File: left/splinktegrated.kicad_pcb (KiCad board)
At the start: 4 copper layers, 72.5 x 88.4 mm, 81 parts, among them J1 USB_C_Receptacle_USB2.0, J10 NA_Ribbon, J13 Conn_01x01_Socket, J14 Cirque, J15 Conn_01x01_Socket, J16 Conn_01x01_Socket, J17 Conn_01x01_Socket, J18 USB_C_Receptacle_USB2.0, J19 Conn_01x01_Socket, J20 Conn_01x01_Socket, J5 Conn_01x02, J6 Cirque, J7 NA_trackball, J8 NA_Ribbon, J9 NA_RGB, Q4 AO3401A, Q5 AO3401A, SW2 NA_SW_SPST, U1 RP2040, U2 USBLC6-2P6, U3 XC6210B332MR-G, U4 USBLC6-2P6, U5 W25Q128JVS, U6 74LVC1T45, Y1 Crystal_GND24

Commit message: move things
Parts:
- removed the H5008 at (173.2, 145.5)
- removed the H5008 at (165.2, 99.7)
- removed the H5008 at (160.6, 126.0)
- removed the H5008 at (131.6, 95.8)
- removed the H5008 at (137.2, 127.2)
- removed the H5008 at (122.7, 145.6)
- removed the H5008 at (130.6, 66.9)
- removed the H5008 at (172.9, 66.9)
- added ?: , , B.Cu at (151.4, 118.7)
- added G***: LOGO, LOGO, F.Cu at (167.4, 96.9)
- added H5008: NA_M4, local-libraries:mousebite, B.Cu at (139.6, 99.7)
- added H5008: NA_M4, local-libraries:mousebite, B.Cu at (131.9, 66.9)
- added H5008: NA_M4, local-libraries:mousebite, B.Cu at (174.3, 66.9)
- added H5008: NA_M4, local-libraries:mousebite, B.Cu at (144.2, 126.0)
- added H5008: NA_M4, local-libraries:mousebite, B.Cu at (173.2, 95.8)
- added H5008: NA_M4, local-libraries:mousebite, B.Cu at (182.2, 145.6)
- added H5008: NA_M4, local-libraries:mousebite, B.Cu at (167.7, 127.2)
- added H5008: NA_M4, local-libraries:mousebite, B.Cu at (131.7, 145.5)
- added J9: NA_RGB, Library:header1x03, B.Cu at (164.8, 103.7)
- added SW2: NA_SW_SPST, Library:PushSwitch, F.Cu at (166.4, 96.8)
- H1, H2, J10, J7, J8: moved to B.Cu
- moved H1 41.6 mm to (173.2, 110.0), turned to 180 degrees
- moved G*** 29.9 mm to (167.4, 96.9), turned to 180 degrees
- moved SW2 28.0 mm to (166.4, 97.0), turned to -90 degrees
- moved H2 27.6 mm to (138.6, 82.1), turned to 180 degrees
- moved D2 11.0 mm to (152.8, 86.7)
- moved D39 11.0 mm to (161.6, 88.8)
- moved F1 11.0 mm to (145.5, 87.0)
- moved F2 11.0 mm to (161.6, 85.9)
- moved FB1 11.0 mm to (156.6, 85.3)
- moved FB13 11.0 mm to (159.6, 85.9)
- moved FB14 11.0 mm to (145.4, 85.2)
- moved FB2 11.0 mm to (170.5, 85.2)
- moved J1 11.0 mm to (150.4, 75.3)
- moved J18 11.0 mm to (165.4, 75.3)
- moved Q4 11.0 mm to (166.5, 86.2)
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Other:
- board size 72.5 x 88.4 mm -> 72.6 x 88.4 mm

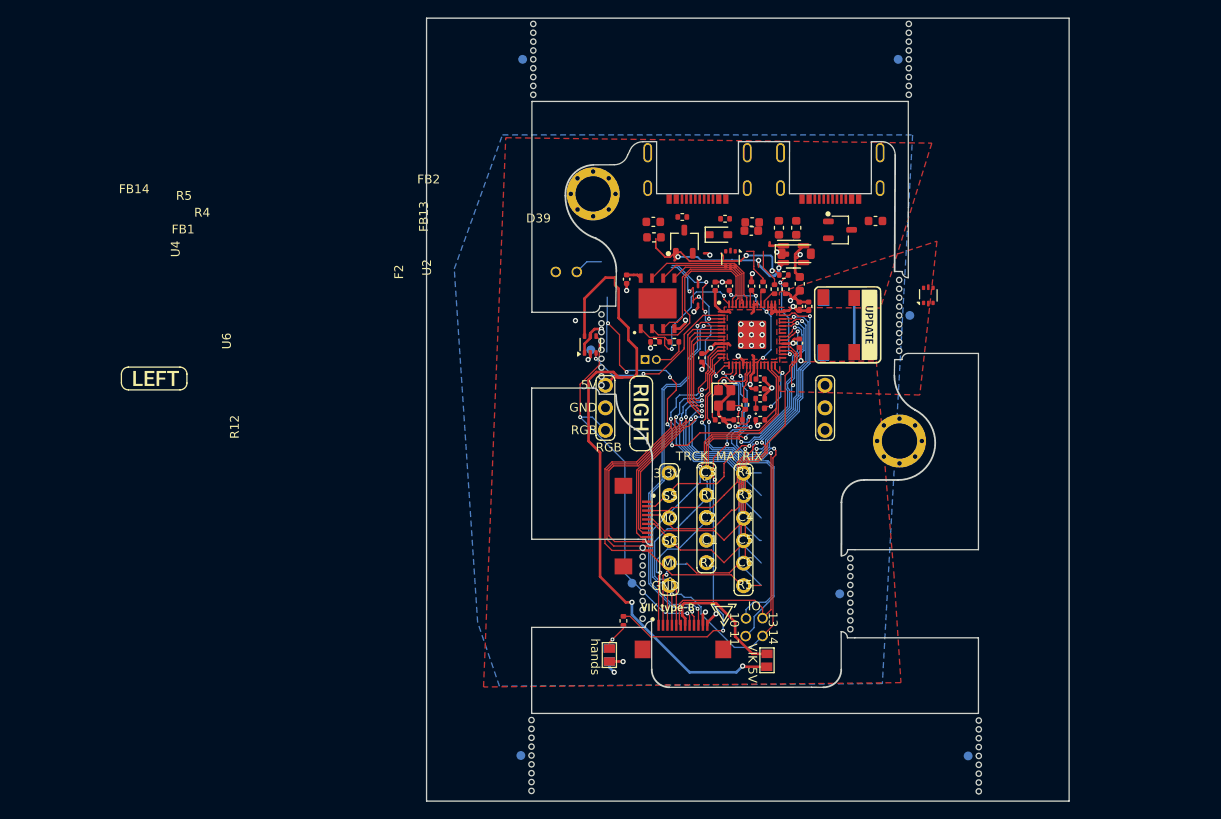
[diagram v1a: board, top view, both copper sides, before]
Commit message: route left side
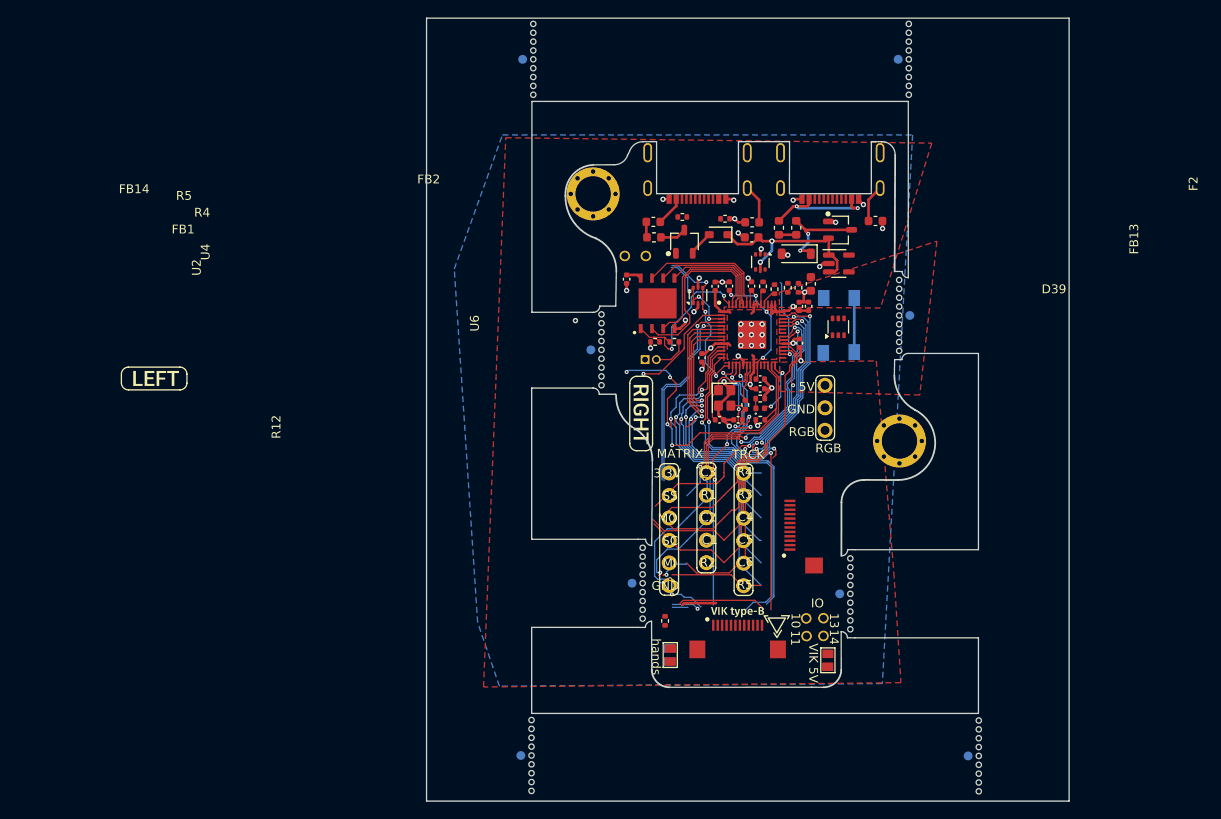
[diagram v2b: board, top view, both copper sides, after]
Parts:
- removed the G*** at (167.4, 96.9)
- removed the J9 at (140.0, 103.7)
- removed the SW2 at (166.4, 96.8)
- moved U6 28.1 mm to (166.3, 97.1)
- moved U2 26.0 mm to (150.5, 93.5)
- moved J14 18.8 mm to (162.2, 119.5), turned to 90 degrees
- moved J19 8.00 mm to (142.2, 89.1)
- moved J20 8.00 mm to (144.6, 89.1)
- moved G*** 7.91 mm to (154.9, 129.3)
- moved J15 6.88 mm to (162.7, 132.0)
- moved J16 6.88 mm to (164.6, 130.0)
- moved J17 6.88 mm to (164.6, 132.0)
- moved NA_JP5 6.88 mm to (165.1, 134.8)
- moved NA_JP7 6.88 mm to (147.3, 134.2)
- moved J13 6.80 mm to (162.7, 130.0)
- moved NA_JP6 6.80 mm to (147.2, 134.2)
- moved J6 6.18 mm to (154.9, 132.2)
- moved G*** 6.14 mm to (159.3, 130.9)
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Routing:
- net VBUS: track 93.5 -> 21.4 mm, vias 5 -> 2
- net rgb_5V: track 43.8 -> 0.00 mm, vias 2 -> 0
- net /D14: track 57.6 -> 23.7 mm
- net row5_l: track 75.3 -> 48.5 mm
- net col5_l: track 56.8 -> 34.6 mm
- net col6_l: track 57.7 -> 38.7 mm, vias 2 -> 3
- net SDA: track 43.0 -> 24.6 mm, vias 2 -> 1
- net SCL: track 42.8 -> 25.4 mm
- net col4_l: track 48.3 -> 31.9 mm
- net ss_l: track 39.8 -> 23.4 mm
- net V_USB_DETECT: track 19.2 -> 2.87 mm, vias 2 -> 0
- net row3_l: track 45.1 -> 29.1 mm
- net /hand: track 45.5 -> 29.7 mm, vias 4 -> 3
- net row4_l: track 43.3 -> 28.9 mm
- net Net-(FB13-Pad1): track 0.00 -> 13.4 mm, vias 0 -> 2
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
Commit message: routing
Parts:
- moved U6 3.35 mm to (166.2, 93.8)
- moved R5 0.50 mm to (148.2, 84.7)
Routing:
- net /D13: track 47.9 -> 13.4 mm, vias 4 -> 3
- net serial_l: track 12.1 -> 42.4 mm, vias 3 -> 6
- net /D10: track 38.1 -> 8.88 mm
- net /~{RESET}: track 34.9 -> 7.09 mm, vias 4 -> 0
- net /D11: track 34.7 -> 7.99 mm
- net serial_l2: track 18.6 -> 44.4 mm, vias 3 -> 5
- net /hand: track 29.7 -> 8.86 mm, vias 3 -> 1
- net /D-: track 0.00 -> 19.7 mm, vias 0 -> 2
- net mosi_l: track 44.8 -> 27.6 mm, vias 4 -> 2
- net rgb_5V: track 0.00 -> 17.2 mm
- net row5_l: track 48.5 -> 31.6 mm, vias 2 -> 1
- net /D+: track 0.00 -> 16.8 mm, vias 0 -> 2
- net VBUS: track 21.4 -> 35.6 mm
- net SCL: track 25.4 -> 12.0 mm, vias 2 -> 1
- net /D14: track 23.7 -> 10.7 mm, vias 5 -> 3
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
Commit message: routing
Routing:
- net /D11: track 7.99 -> 52.3 mm, vias 1 -> 3
- net /D10: track 8.88 -> 51.1 mm
- net /D14: track 10.7 -> 52.3 mm, vias 3 -> 6
- net SCL: track 12.0 -> 49.6 mm, vias 1 -> 2
- net SDA: track 12.5 -> 49.7 mm, vias 1 -> 2
- net VBUS: track 35.6 -> 72.1 mm
- net /D13: track 13.4 -> 48.9 mm, vias 3 -> 4
- net rgb_5V: track 17.2 -> 50.8 mm, vias 0 -> 2
- net /hand: track 8.86 -> 36.4 mm, vias 1 -> 2
- net row1_l: track 33.4 -> 60.9 mm, vias 2 -> 4
- net col2_l: track 33.6 -> 59.1 mm, vias 2 -> 4
- net col1_l: track 36.0 -> 59.2 mm, vias 2 -> 4
- net /~{RESET}: track 7.09 -> 30.1 mm, vias 0 -> 3
- net row4_l: track 20.7 -> 42.5 mm
- net rgb_3v3: track 0.00 -> 20.9 mm, vias 0 -> 2
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
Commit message: routing
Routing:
- net col1_l: track 59.2 -> 61.5 mm
- net col2_l: track 59.1 -> 61.3 mm
- net miso_l: track 42.1 -> 40.5 mm
- net col4_l: track 43.1 -> 44.5 mm
- net sc_l: track 45.2 -> 44.2 mm
- net mosi_l: track 41.9 -> 41.1 mm
- net /D11: track 52.3 -> 52.9 mm

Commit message: silkscreen
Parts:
- added kibuzzard-6208EFFE: G***, kibuzzard-6208EFFE, B.Cu at (146.0, 105.1)
- moved kibuzzard-6208EFFE 56.7 mm to (146.0, 105.1), turned to 90 degrees
- moved kibuzzard-61F01B61 38.9 mm to (107.9, 121.4) (x2)
- moved G*** 21.0 mm to (162.9, 116.5)
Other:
- board text removed: "REV1.4"
